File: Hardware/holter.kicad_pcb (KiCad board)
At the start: 6 copper layers, 33.5 x 48 mm, 262 parts, among them CN1 2TAP, CN2 2TAP, CN3 3TAP, IC1 256kx8, M1 USB_Power_Module, M2 USB_Power_Module, P1 CONN_01X07, P2 PROG, P3 SCREW, P4 BAT-, Q1 PMF170XP, Q2 PMF170XP, Q3 NTR4101PT1G, Q4 PMF170XP, Q5 PMF170XP, U1 TXB0106, U10 TS5A3159, U11 TS5A3159, U12 ESD_PROTECTOR, U13 ESD_PROTECTOR, U14 ESD_PROTECTOR, U15 ESD_PROTECTOR, U16 ESD_PROTECTOR, U17 ESD_PROTECTOR, U18 ESD_PROTECTOR, U19 ESD_PROTECTOR, U2 TXB0106, U20 ESD_PROTECTOR, U21 ESD_PROTECTOR, U22 ESD_PROTECTOR, U23 ESD_PROTECTOR, U24 TLV61220, U25 TLV61220, U26 TLV61220, U27 LM3671, U28 DS2710, U29 LIS2DH12, U3 TiWi-uB2, U4 STM32F4x1_64, U5 uSD, U6 ADS1298, U7 USBULC6-2M6, U8 USB2641, U9 OPA379, X1 32768, Y1 24 MHz, Y2 10 MHz

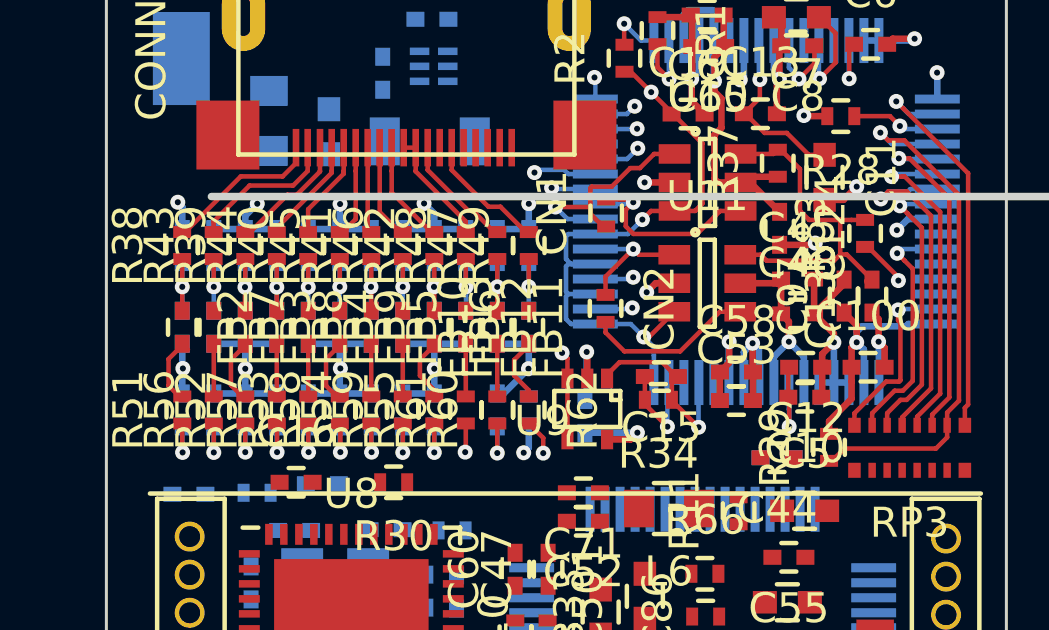
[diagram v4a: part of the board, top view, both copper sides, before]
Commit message: Connected ECG signals to the AD.
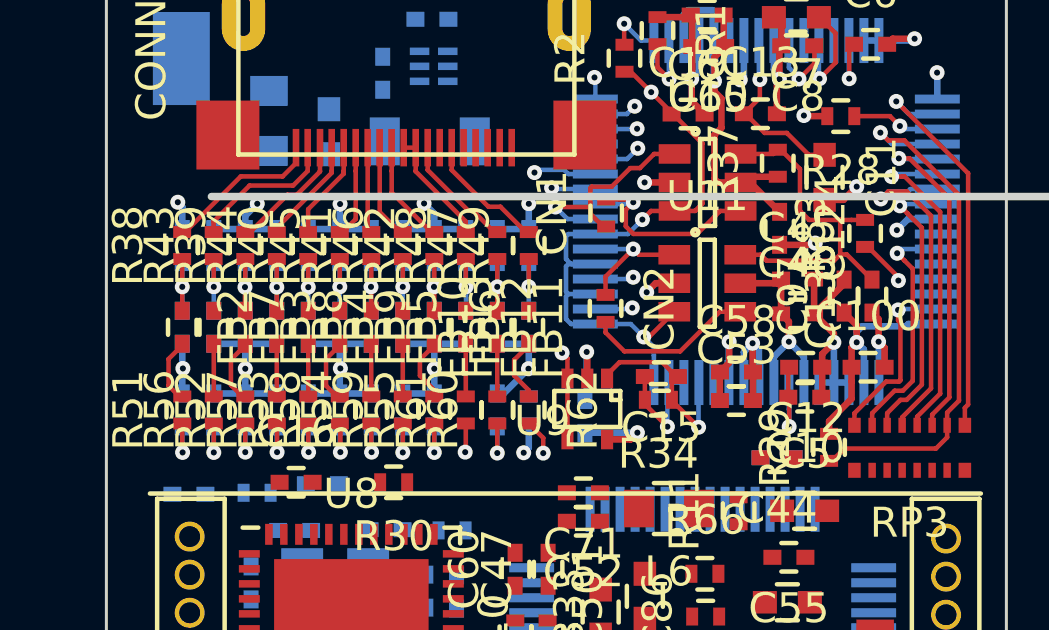
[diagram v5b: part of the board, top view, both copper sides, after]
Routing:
- net V6_F: track 2.57 -> 21.0 mm
- net V1_F: track 3.09 -> 20.1 mm
- net LA_F: track 3.22 -> 19.8 mm
- net V2_F: track 3.29 -> 18.9 mm
- net LL_F: track 3.39 -> 18.1 mm
- net RA_F: track 5.81 -> 19.0 mm
- net V4_F: track 6.44 -> 18.6 mm
- net V3_F: track 9.32 -> 21.2 mm
- net V5_F: track 3.12 -> 12.4 mm
- net RLD_UF: track 5.88 -> 12.4 mm
- net SHIELD_UF: track 4.03 -> 8.88 mm

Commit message: Routing attempt.
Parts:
- moved C3 0.67 mm to (91.5, 61.5)
- moved C50 0.57 mm to (97.1, 56.5)
- moved C86 0.50 mm to (91.8, 56.5)
- moved R66 0.48 mm to (94.7, 56.0)
- moved C4 0.47 mm to (96.6, 61.6)
- moved C55 0.46 mm to (97.6, 55.4)
- moved R68 0.42 mm to (94.7, 57.3)
- moved R31 0.40 mm to (80.0, 52.5)
- moved R30 0.29 mm to (84.9, 52.5)
- moved C501 0.20 mm to (93.0, 56.5)
- moved Y2 0.18 mm to (94.0, 61.5)
- moved U25 0.15 mm to (97.8, 58.9)
- moved C17 0.08 mm to (82.1, 52.5)
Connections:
- M1 pad 11: +3V3 -> ~CHRG_STAT
- M1 pad 12: ~CHRG_STAT -> ~CHRG_EN
- M1 pad 13: ~CHRG_EN -> EN_3V3
- M1 pad 4: Net-(M1-Pad3) -> +3V3
- M2 pad 11: +3.3VP -> /Power/USB Power/~CHRG_STAT
- M2 pad 12: /Power/USB Power/~CHRG_STAT -> /Power/USB Power/~CHRG_EN
- M2 pad 13: /Power/USB Power/~CHRG_EN -> /Power/USB Power/EN_3V3
- M2 pad 4: /Power/USB Power/BAT- -> +3.3VP
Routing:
- net GND: track 75.1 -> 173.1 mm, vias 25 -> 40
- net BAT+: track 0.00 -> 35.8 mm, vias 0 -> 3
- net Net-(RP2-Pad1): track 0.00 -> 22.8 mm, vias 0 -> 2
- net +5V: track 0.00 -> 22.8 mm, vias 0 -> 1
- net VMEM: track 0.00 -> 20.7 mm, vias 0 -> 2
- net +3V3: track 0.00 -> 19.4 mm, vias 0 -> 6
- net DP: track 0.00 -> 18.4 mm, vias 0 -> 1
- net DM: track 0.00 -> 18.3 mm, vias 0 -> 1
- net +2.8VD: track 0.00 -> 17.2 mm, vias 0 -> 2
- net Net-(RP2-Pad2): track 0.00 -> 16.6 mm, vias 0 -> 2
- net Net-(RP2-Pad3): track 0.00 -> 16.1 mm, vias 0 -> 2
- net Net-(RP2-Pad4): track 0.00 -> 15.3 mm, vias 0 -> 2
- net Net-(RP2-Pad5): track 0.00 -> 13.8 mm, vias 0 -> 2
- net Net-(C4-Pad2): track 0.00 -> 12.6 mm, vias 0 -> 2
- net EN_3V3: track 0.00 -> 11.9 mm
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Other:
- net class 1A added: clearance 0.1524, trace_width 0.7, via_dia 0.7, via_drill 0.4
- net class High Current: trace_width 1.5 -> 1.22

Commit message: Routing attempt.
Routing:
- net VCPU: track 10.3 -> 34.8 mm, vias 3 -> 5
- net +2.8VA: track 30.3 -> 48.5 mm
- net ~ECG_PWDN: track 4.24 -> 22.2 mm
- net +3V3: track 19.4 -> 37.1 mm, vias 6 -> 7
- net +1V8: track 15.5 -> 28.4 mm
- net ~ECG_RST: track 2.57 -> 13.2 mm
- net DIFF_SEL: track 3.01 -> 13.5 mm
- net ECG_START: track 2.61 -> 12.0 mm
- net ~ECG_DRDY: track 2.11 -> 9.63 mm
- net GND: track 173.1 -> 179.6 mm, vias 40 -> 41
- net SD_CPU: track 0.96 -> 4.87 mm, vias 1 -> 2
- net Net-(C5-Pad1): track 0.00 -> 3.11 mm, vias 0 -> 1
- net ~CARD_DET: track 0.00 -> 1.38 mm, vias 0 -> 1

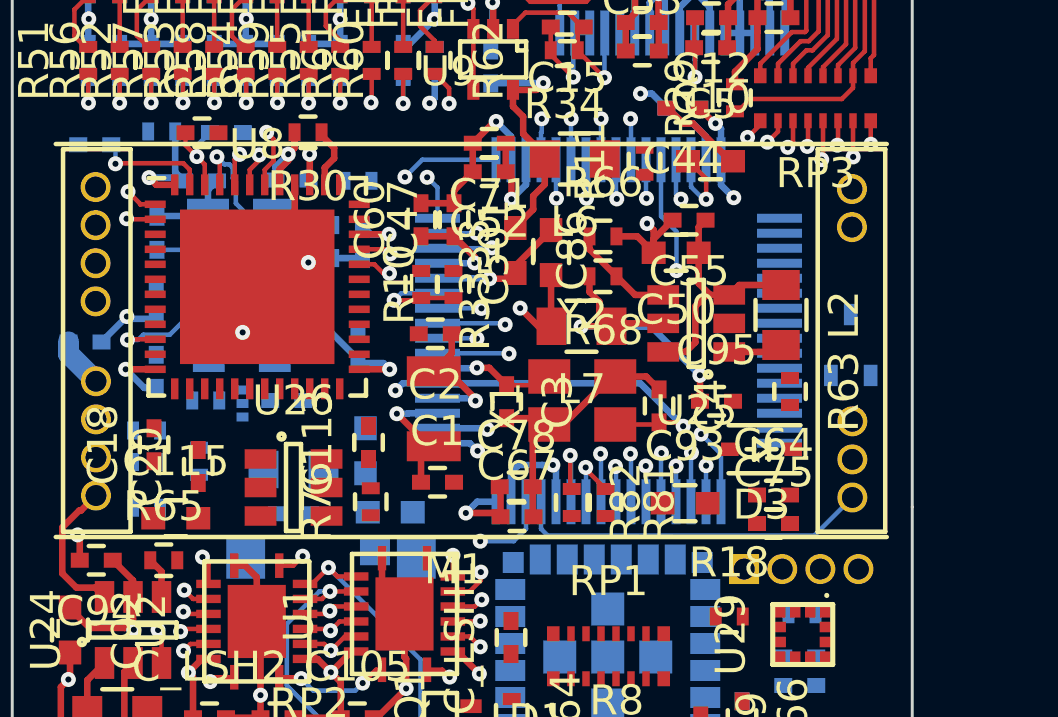
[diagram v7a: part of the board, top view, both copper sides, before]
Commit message: Fix QFN48 footprint. Another routing attempt.
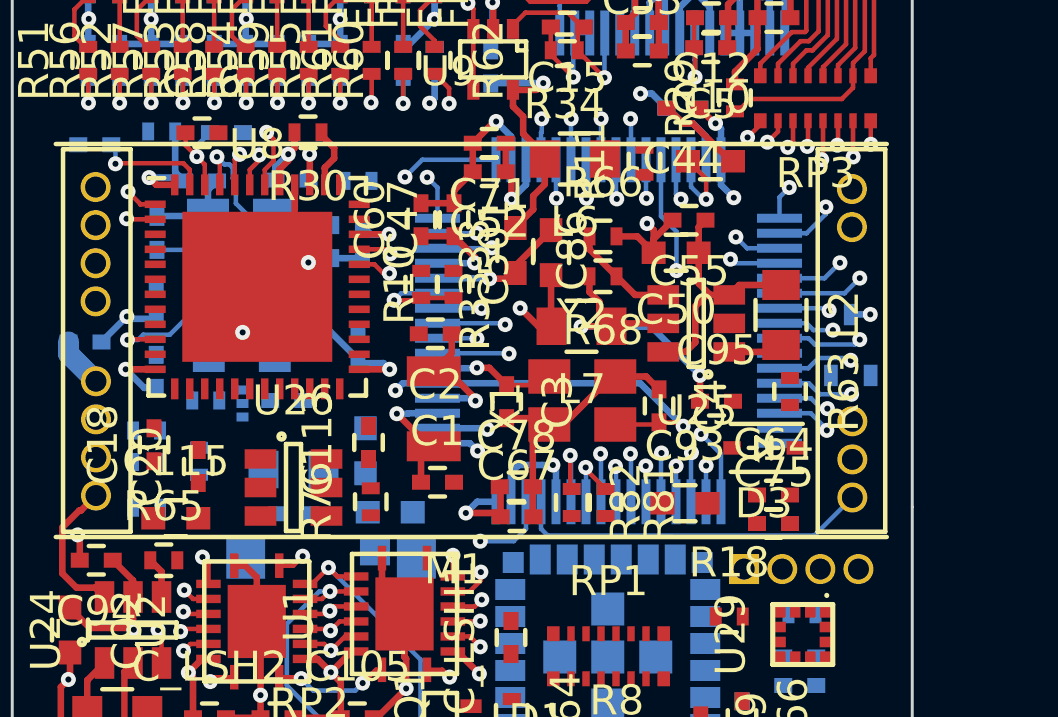
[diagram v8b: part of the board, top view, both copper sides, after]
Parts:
- U8: footprint Housings_DFN_QFN:QFN-48-1EP_7x7mm_Pitch0.5mm -> Footprints:QFN-48-1EP_7x7mm_Pitch0.5mm
- moved D3 0.09 mm to (100.0, 63.0)
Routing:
- net +1V8: track 28.4 -> 63.2 mm, vias 5 -> 6
- net GND: track 179.6 -> 165.8 mm
- net ACC_INT: track 0.00 -> 2.88 mm, vias 0 -> 1
- net 32768_CLK: track 0.00 -> 2.83 mm, vias 0 -> 1
- net MCU_USB_DM: track 1.09 -> 3.64 mm, vias 1 -> 2
- net ADCLK: track 0.82 -> 3.37 mm, vias 1 -> 2
- net ACC_PWR: track 0.00 -> 2.23 mm, vias 0 -> 1
- net ACC_CLK: track 0.00 -> 2.04 mm, vias 0 -> 1
- net SDIO_D1: track 1.36 -> 3.24 mm, vias 1 -> 2
- net SWDIO: track 0.00 -> 1.83 mm, vias 0 -> 1
- net MCU_USB_DP: track 0.96 -> 2.70 mm, vias 1 -> 2
- net ACC_MOSI: track 0.00 -> 1.69 mm, vias 0 -> 1
- net SDIO_D0: track 0.71 -> 2.39 mm, vias 1 -> 2
- net ACC_MISO: track 0.00 -> 1.61 mm, vias 0 -> 1
- net ACC_CS: track 0.00 -> 1.16 mm, vias 0 -> 1
